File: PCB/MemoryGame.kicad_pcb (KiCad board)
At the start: 2 copper layers, 50 x 60 mm, 25 parts, among them SW1 SW_SPDT, SW2 bt_red, SW3 bt_blue, SW4 bt_yellow, SW5 bt_green, X1 Arduino_Pro_Mini

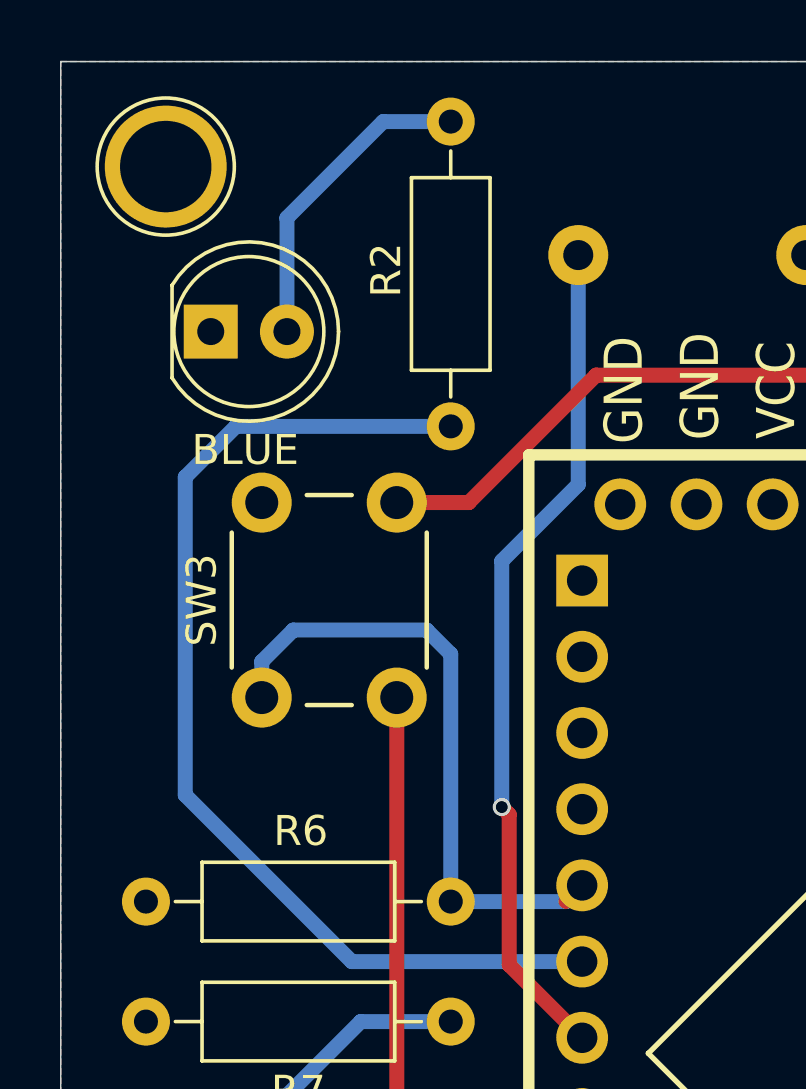
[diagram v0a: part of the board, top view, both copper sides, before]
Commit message: PCB minor update
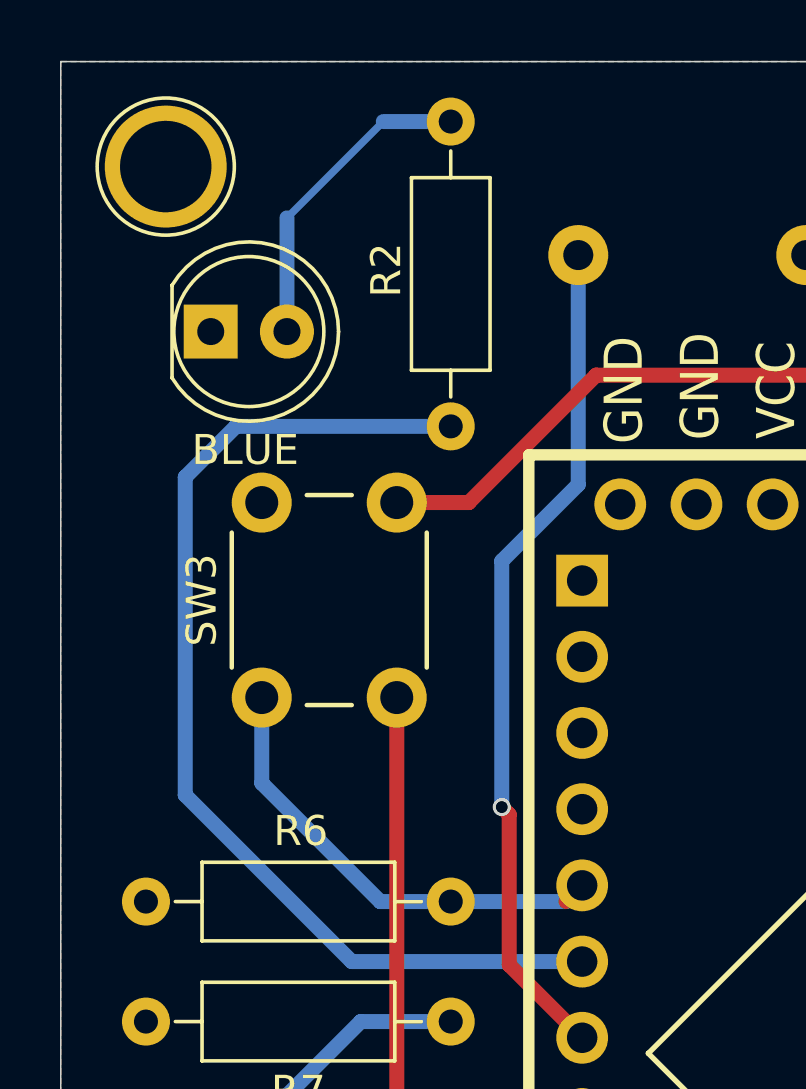
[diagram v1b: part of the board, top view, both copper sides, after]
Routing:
- net Bt_Blue: track 21.9 -> 16.2 mm
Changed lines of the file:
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@@
     (thickness 1.6)
     (drawings 14)
-    (tracks 85)
+    (tracks 83)
     (zones 0)
     (modules 25)
@@
   (page A4)
   (layers
-    (0 F.Cu signal hide)
-    (31 B.Cu signal hide)
+    (0 F.Cu signal)
+    (31 B.Cu signal)
     (32 B.Adhes user)
     (33 F.Adhes user)
@@
     (visible_elements FFFEFF7F)
     (pcbplotparams
-      (layerselection 0x00030_80000001)
-      (usegerberextensions false)
+      (layerselection 0x010f0_80000001)
+      (usegerberextensions true)
       (excludeedgelayer true)
       (linewidth 0.100000)
@@
       (drillshape 0)
       (scaleselection 1)
-      (outputdirectory ""))
+      (outputdirectory gerbers/))
   )
   (net 0 "")
@@
   (segment (start 157.2 112.7) (end 159.7 115.2) (width 0.5) (layer B.Cu) (net 8))
   (segment (start 159.7 108.7) (end 160.3 108.7) (width 0.5) (layer F.Cu) (net 8))
-  (segment (start 126.7 91.2) (end 126.7 90) (width 0.5) (layer B.Cu) (net 9))
-  (segment (start 133 89.75) (end 133 98) (width 0.5) (layer B.Cu) (net 9))
-  (segment (start 132.2 88.95) (end 133 89.75) (width 0.5) (layer B.Cu) (net 9))
-  (segment (start 127.75 88.95) (end 132.2 88.95) (width 0.5) (layer B.Cu) (net 9))
-  (segment (start 126.7 90) (end 127.75 88.95) (width 0.5) (layer B.Cu) (net 9))
+  (segment (start 126.7 91.2) (end 126.7 94.05) (width 0.5) (layer B.Cu) (net 9))
+  (segment (start 130.65 98) (end 133 98) (width 0.5) (layer B.Cu) (net 9))
+  (segment (start 126.7 94.05) (end 130.65 98) (width 0.5) (layer B.Cu) (net 9))
   (segment (start 133 98) (end 136.84 98) (width 0.5) (layer B.Cu) (net 9))
   (segment (start 136.84 98) (end 137.38 97.46) (width 0.5) (layer B.Cu) (net 9))
@@
   (segment (start 133 72) (end 130.75 72) (width 0.5) (layer B.Cu) (net 34))
   (segment (start 127.54 75.21) (end 127.54 79) (width 0.5) (layer B.Cu) (net 34))
-  (segment (start 130.75 72) (end 127.54 75.21) (width 0.5) (layer B.Cu) (net 34))
+  (segment (start 130.75 72) (end 127.54 75.21) (width 0.25) (layer B.Cu) (net 34))
   (segment (start 158 72) (end 160 72) (width 0.5) (layer B.Cu) (net 35))
   (segment (start 165.54 77.54) (end 165.54 79) (width 0.5) (layer B.Cu) (net 35))

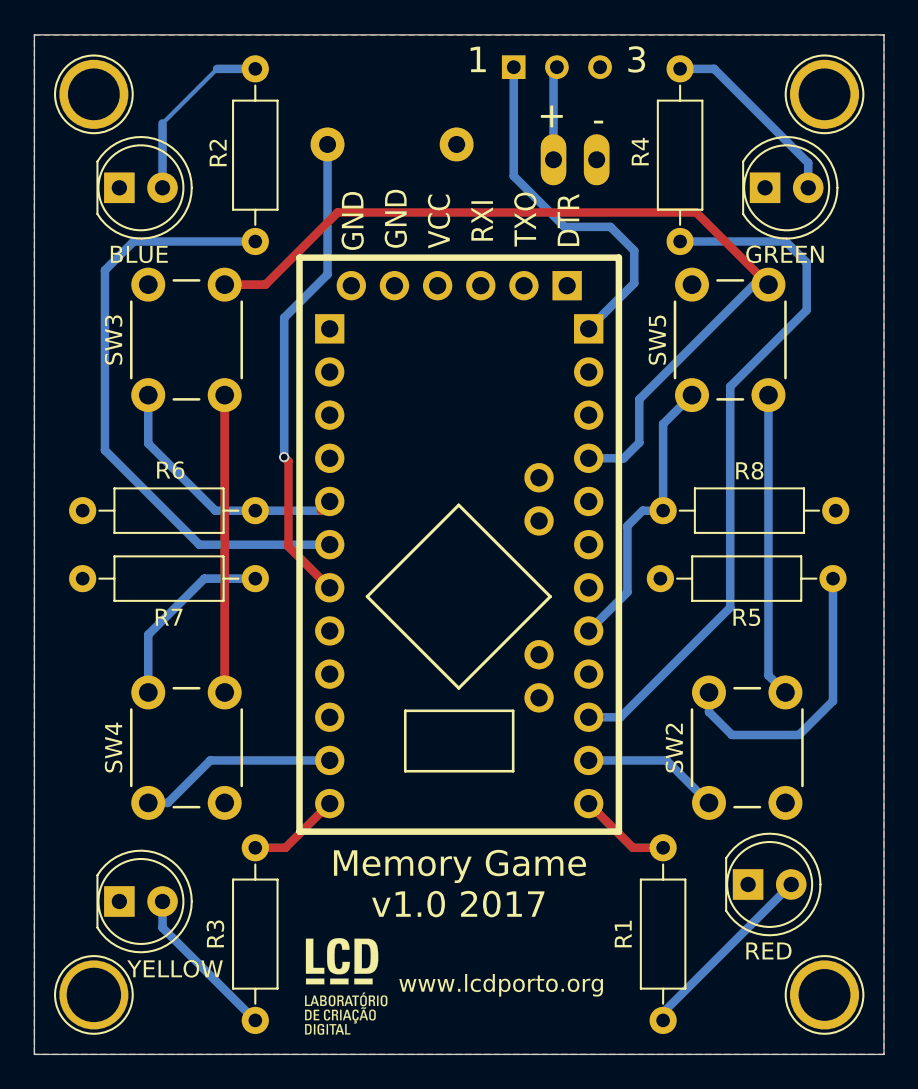
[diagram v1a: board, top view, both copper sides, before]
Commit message: minor changes in components position
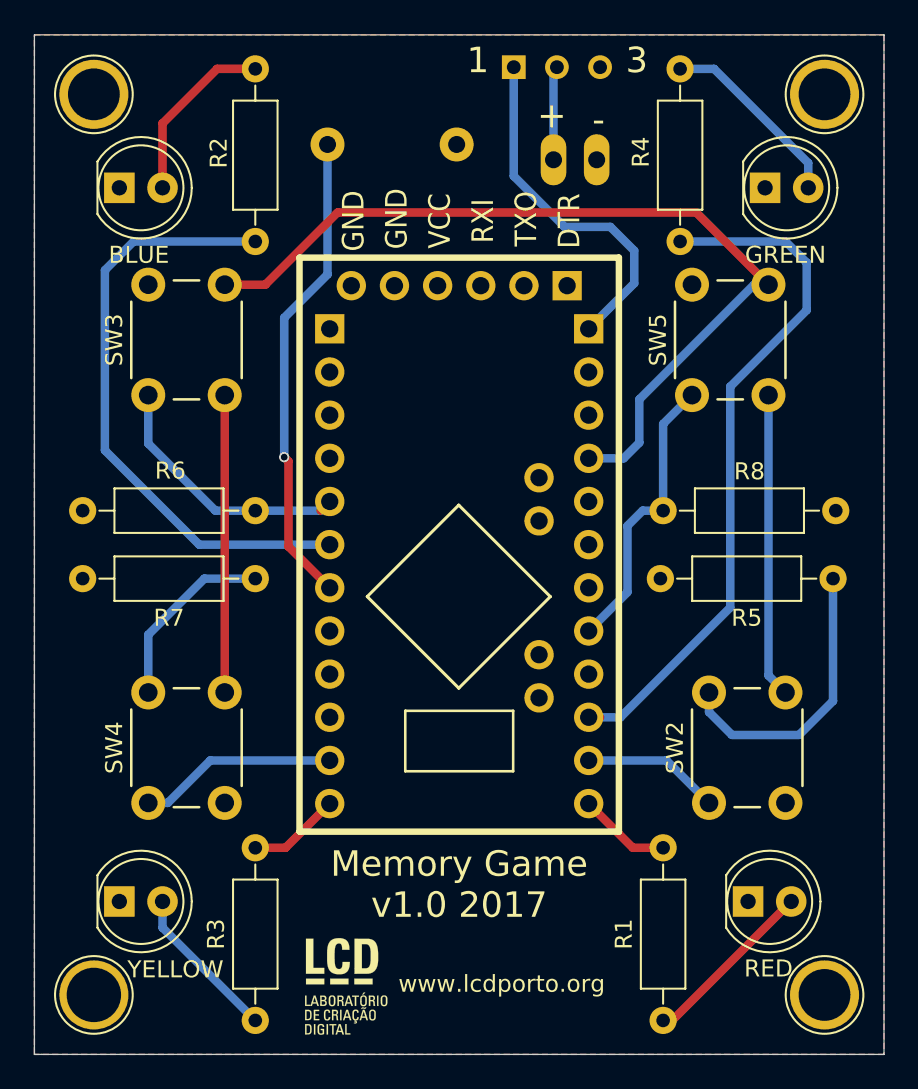
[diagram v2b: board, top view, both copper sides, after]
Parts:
- moved RED 1.00 mm to (162.0, 121.0)
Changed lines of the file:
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@@
     (thickness 1.6)
     (drawings 14)
-    (tracks 83)
+    (tracks 84)
     (zones 0)
     (modules 25)
@@
   )
   (setup
-    (last_trace_width 0.25)
+    (last_trace_width 0.5)
     (user_trace_width 0.2)
     (user_trace_width 0.3)
@@
   )
   (module LEDs:LED_D5.0mm (layer F.Cu)
-    (at 162 120)
+    (at 162 121)
     (descr "LED, diameter 5.0mm, 2 pins, http://cdn-reichelt.de/documents/datenblatt/A500/LL-504BC2E-009.pdf")
     (tags "LED diameter 5.0mm 2 pins")
@@
   (segment (start 163.2 91.2) (end 163.2 107.7) (width 0.5) (layer B.Cu) (net 14))
   (segment (start 163.2 107.7) (end 164.2 108.7) (width 0.5) (layer B.Cu) (net 14))
-  (segment (start 133 72) (end 130.75 72) (width 0.5) (layer B.Cu) (net 34))
-  (segment (start 127.54 75.21) (end 127.54 79) (width 0.5) (layer B.Cu) (net 34))
-  (segment (start 130.75 72) (end 127.54 75.21) (width 0.25) (layer B.Cu) (net 34))
+  (segment (start 127.54 79) (end 127.54 75.21) (width 0.5) (layer F.Cu) (net 34) (status 400000))
+  (segment (start 130.75 72) (end 133 72) (width 0.5) (layer F.Cu) (net 34) (status 800000))
+  (segment (start 127.54 75.21) (end 130.75 72) (width 0.5) (layer F.Cu) (net 34))
   (segment (start 158 72) (end 160 72) (width 0.5) (layer B.Cu) (net 35))
   (segment (start 165.54 77.54) (end 165.54 79) (width 0.5) (layer B.Cu) (net 35))
   (segment (start 160 72) (end 165.54 77.54) (width 0.5) (layer B.Cu) (net 35))
+  (segment (start 157 128) (end 157.54 128) (width 0.5) (layer F.Cu) (net 36) (status C00000))
+  (segment (start 157.54 128) (end 164.54 121) (width 0.5) (layer F.Cu) (net 36) (status C00000))
   (segment (start 157 128) (end 157 127.54) (width 0.5) (layer B.Cu) (net 36))
-  (segment (start 157 127.54) (end 164.54 120) (width 0.5) (layer B.Cu) (net 36))
   (segment (start 127.54 121) (end 127.54 122.54) (width 0.5) (layer B.Cu) (net 37))
   (segment (start 127.54 122.54) (end 133 128) (width 0.5) (layer B.Cu) (net 37))
